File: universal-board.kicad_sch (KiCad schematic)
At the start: 47 parts, among them J1 USB_C_Receptacle, J2 Conn_02x04_Odd_Even, J3 Conn_01x08, J4 CONN_WS2812, J5 CONN_I2C_GROVE, Q1 BSS138, SW1 SW_RESET, SW2 SW_ACK, U1 USBLC6-2SC6, U2 AMS1117-3.3, U3 CH224K, U4 USBLC6-2SC6, U5 74AHCT1G125, U6 TSOP384xx, U7 ESP32-S3-WROOM-1

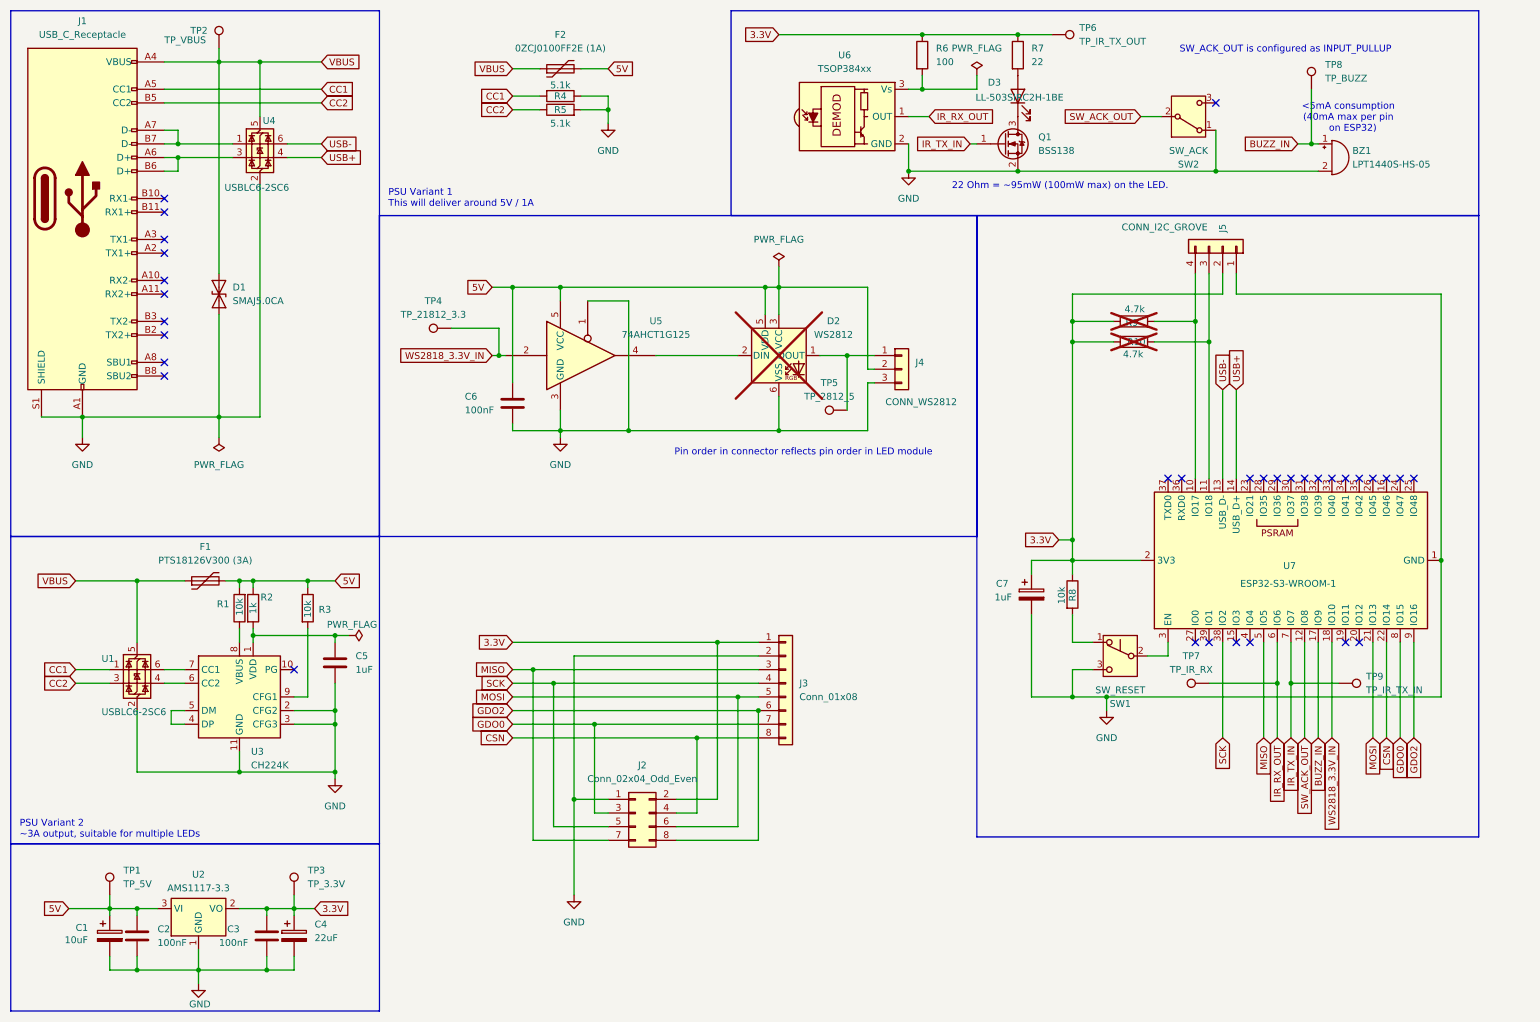
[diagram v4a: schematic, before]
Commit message: Added UART for HLK modules.
Updated TODO.
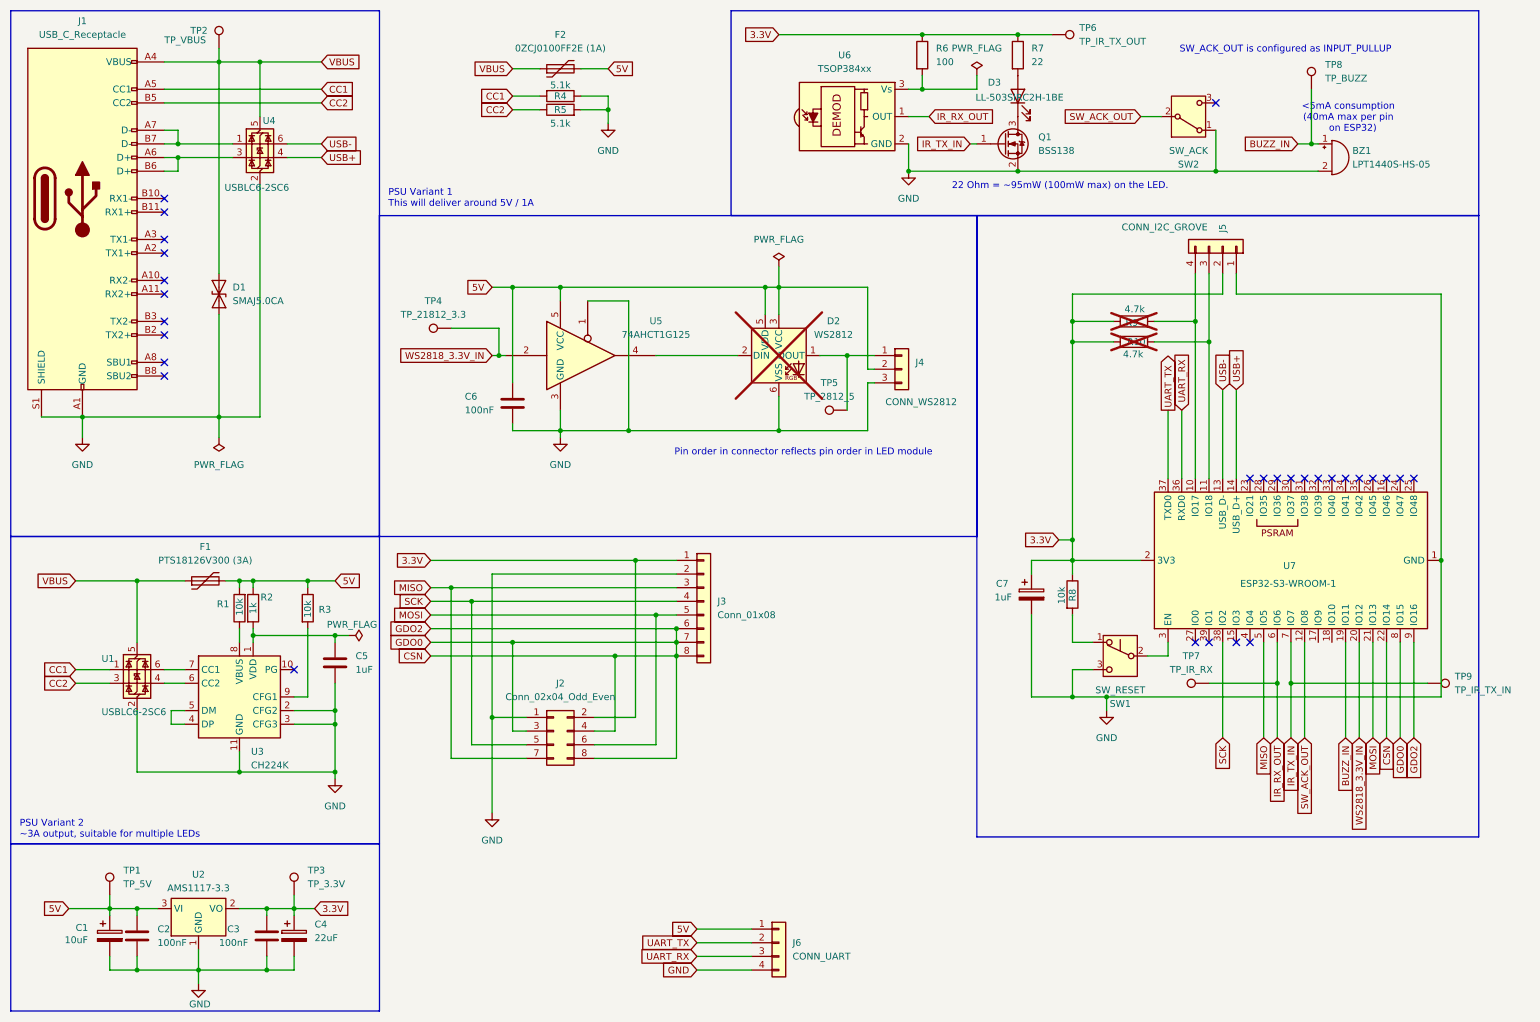
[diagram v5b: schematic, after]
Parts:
- added J6: CONN_UART, symbol Connector_Generic:Conn_01x04
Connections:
- net GDO0 is gone; now on net CSN: J2.3 (Pin_3), J3.7 (Pin_7), U7.8 (IO15)
- net GDO2 is gone; now on net CSN: J2.8 (Pin_8), J3.6 (Pin_6), U7.9 (IO16)
- net 5V: now also J6.1 (Pin_1)
- net BUZZ_IN: now also U7.19 (IO11); no longer U7.17 (IO9)
- net GND: now also J6.4 (Pin_4)
- net WS2818_3.3V_IN: now also U7.20 (IO12); no longer U7.18 (IO10)
- net UART_RX: now reaches U7.36 (RXD0)
- net UART_RX: now also J6.3 (Pin_3)
- net UART_TX: now reaches U7.37 (TXD0)
- net UART_TX: now also J6.2 (Pin_2)
- no-connect marks 33 -> 29
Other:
- moved on the sheet: J2, J3, TP9

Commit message: Changed resistor footprints to be actual resistors.
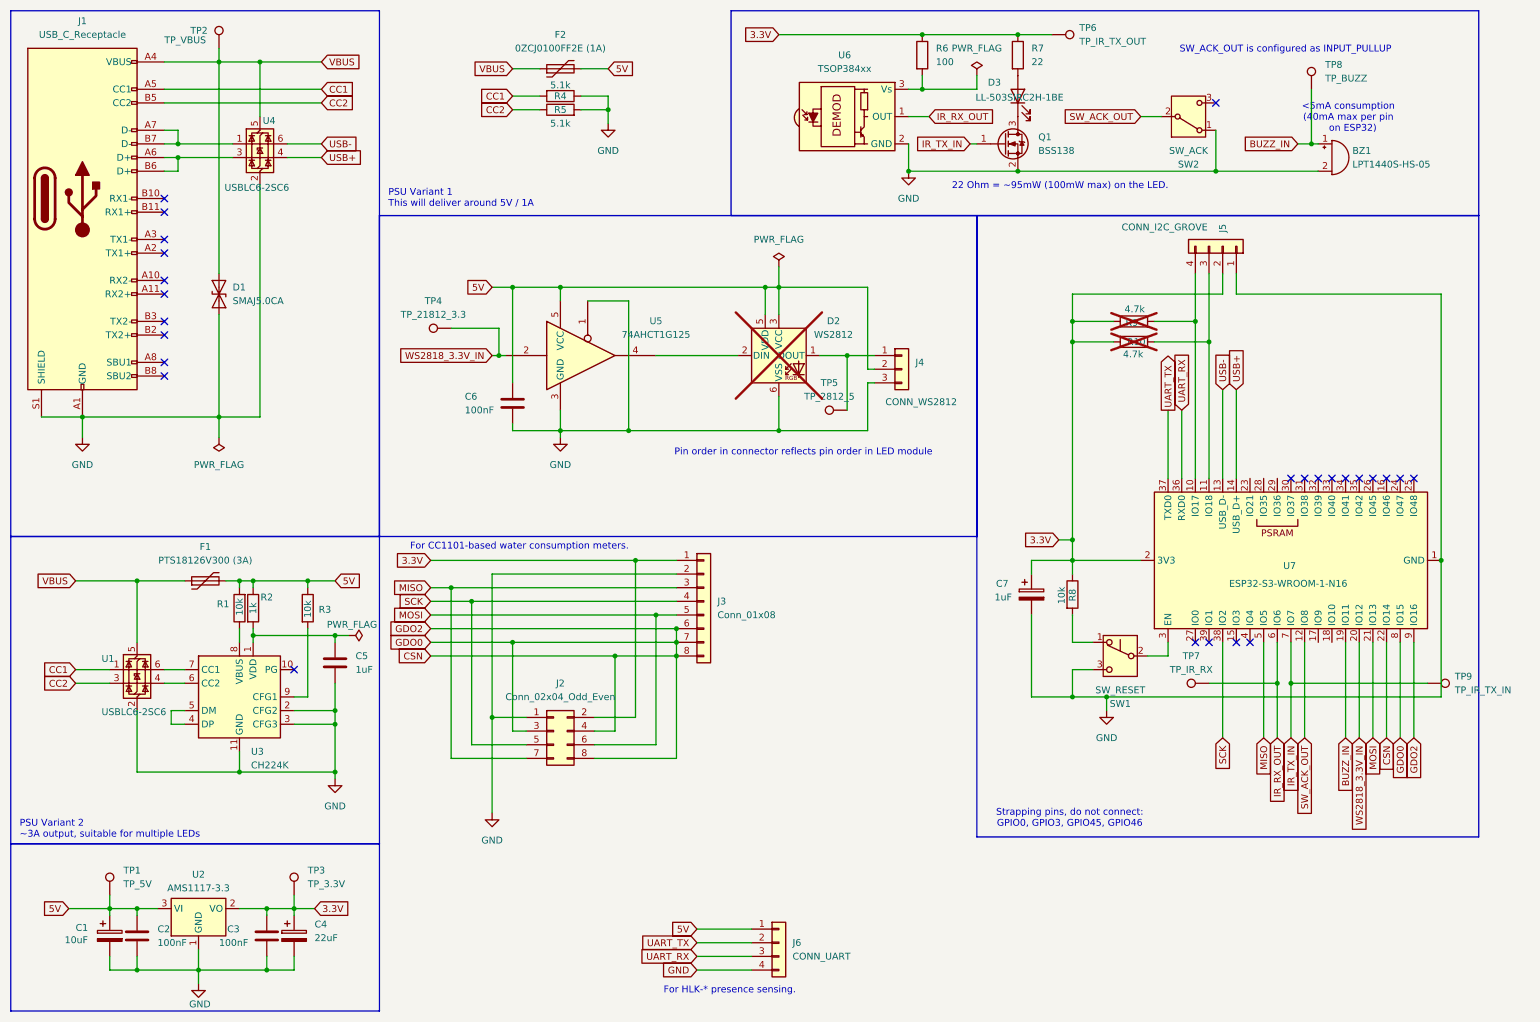
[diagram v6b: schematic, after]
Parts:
- R1, R10, R2, R3, R4, R5, R6, R7, R8, R9: footprint Capacitor_SMD:C_1206_3216Metric_Pad1.33x1.80mm_HandSolder -> Resistor_SMD:R_1206_3216Metric_Pad1.30x1.75mm_HandSolder
- U7: value ESP32-S3-WROOM-1 -> ESP32-S3-WROOM-1-N16
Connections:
- no-connect marks 29 -> 26
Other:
- note added: "For CC1101-based water consumption meters."
- note added: "For HLK-* presence sensing."
- note added: "Strapping pins, do not connect: GPIO0, GPIO3, GPIO45, GPIO46"
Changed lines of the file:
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@@
 		)
 	)
+	(text "For CC1101-based water consumption meters."
+		(exclude_from_sim no)
+		(at 106.68 111.76 0)
+		(effects
+			(font
+				(size 1.27 1.27)
+			)
+		)
+	)
 	(text "<5mA consumption\n(40mA max per pin\n   on ESP32)\n"
 		(exclude_from_sim no)
@@
 		)
 	)
+	(text "Strapping pins, do not connect:\nGPIO0, GPIO3, GPIO45, GPIO46"
+		(exclude_from_sim no)
+		(at 209.042 162.306 0)
+		(effects
+			(font
+				(size 1.27 1.27)
+			)
+		)
+	)
+	(text "For HLK-* presence sensing."
+		(exclude_from_sim no)
+		(at 145.796 194.31 0)
+		(effects
+			(font
+				(size 1.27 1.27)
+			)
+		)
+	)
 	(text "Pin order in connector reflects pin order in LED module"
 		(exclude_from_sim no)
@@
 	)
 	(no_connect
-		(at 247.65 99.06)
-	)
-	(no_connect
 		(at 267.97 99.06)
 	)
 	(no_connect
-		(at 245.11 99.06)
-	)
-	(no_connect
 		(at 40.64 72.39)
 	)
@@
 		(at 240.03 129.54)
 	)
-	(no_connect
-		(at 242.57 99.06)
-	)
 	(wire
 		(pts
@@
 			)
 		)
-		(property "Footprint" "Capacitor_SMD:C_1206_3216Metric_Pad1.33x1.80mm_HandSolder"
+		(property "Footprint" "Resistor_SMD:R_1206_3216Metric_Pad1.30x1.75mm_HandSolder"
 			(at 207.772 120.65 90)
 			(effects
@@
 			)
 		)
-		(property "Footprint" "Capacitor_SMD:C_1206_3216Metric_Pad1.33x1.80mm_HandSolder"
+		(property "Footprint" "Resistor_SMD:R_1206_3216Metric_Pad1.30x1.75mm_HandSolder"
 			(at 197.612 20.32 90)
 			(effects
@@
 			)
 		)
-		(property "Footprint" "Capacitor_SMD:C_1206_3216Metric_Pad1.33x1.80mm_HandSolder"
+		(property "Footprint" "Resistor_SMD:R_1206_3216Metric_Pad1.30x1.75mm_HandSolder"
 			(at 55.372 123.19 90)
 			(effects
@@
 			)
 		)
-		(property "Value" "ESP32-S3-WROOM-1"
+		(property "Value" "ESP32-S3-WROOM-1-N16"
 			(at 249.682 118.618 90)
 			(effects
@@
 			)
 		)
-		(property "Footprint" "Capacitor_SMD:C_1206_3216Metric_Pad1.33x1.80mm_HandSolder"
+		(property "Footprint" "Resistor_SMD:R_1206_3216Metric_Pad1.30x1.75mm_HandSolder"
 			(at 220.98 71.628 90)
 			(effects
@@
 			)
 		)
-		(property "Footprint" "Capacitor_SMD:C_1206_3216Metric_Pad1.33x1.80mm_HandSolder"
+		(property "Footprint" "Resistor_SMD:R_1206_3216Metric_Pad1.30x1.75mm_HandSolder"
 			(at 220.98 71.882 90)
 			(effects
@@
 			)
 		)
-		(property "Footprint" "Capacitor_SMD:C_1206_3216Metric_Pad1.33x1.80mm_HandSolder"
+		(property "Footprint" "Resistor_SMD:R_1206_3216Metric_Pad1.30x1.75mm_HandSolder"
 			(at 56.388 123.19 90)
 			(effects
@@
 			)
 		)
-		(property "Footprint" "Capacitor_SMD:C_1206_3216Metric_Pad1.33x1.80mm_HandSolder"
+		(property "Footprint" "Resistor_SMD:R_1206_3216Metric_Pad1.30x1.75mm_HandSolder"
 			(at 114.3 32.258 90)
 			(effects
@@
 			)
 		)
-		(property "Footprint" "Capacitor_SMD:C_1206_3216Metric_Pad1.33x1.80mm_HandSolder"
+		(property "Footprint" "Resistor_SMD:R_1206_3216Metric_Pad1.30x1.75mm_HandSolder"
 			(at 114.3 26.162 90)
 			(effects
@@
 			)
 		)
-		(property "Footprint" "Capacitor_SMD:C_1206_3216Metric_Pad1.33x1.80mm_HandSolder"
+		(property "Footprint" "Resistor_SMD:R_1206_3216Metric_Pad1.30x1.75mm_HandSolder"
 			(at 179.832 20.32 90)
 			(effects
@@
 			)
 		)
-		(property "Footprint" "Capacitor_SMD:C_1206_3216Metric_Pad1.33x1.80mm_HandSolder"
+		(property "Footprint" "Resistor_SMD:R_1206_3216Metric_Pad1.30x1.75mm_HandSolder"
 			(at 65.532 123.19 90)
 			(effects

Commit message: Added footprint for GCT USB4105-GF-A
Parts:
- J1: footprint Connector_USB:USB_C_Receptacle_GCT_USB4085 -> Connector_USB:USB_C_Receptacle_GCT_USB4105-xx-A_16P_TopMnt_Horizontal
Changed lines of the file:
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@@
 			)
 		)
-		(property "Footprint" "Connector_USB:USB_C_Receptacle_GCT_USB4085"
+		(property "Footprint" "Connector_USB:USB_C_Receptacle_GCT_USB4105-xx-A_16P_TopMnt_Horizontal"
 			(at 29.21 46.99 0)
 			(effects

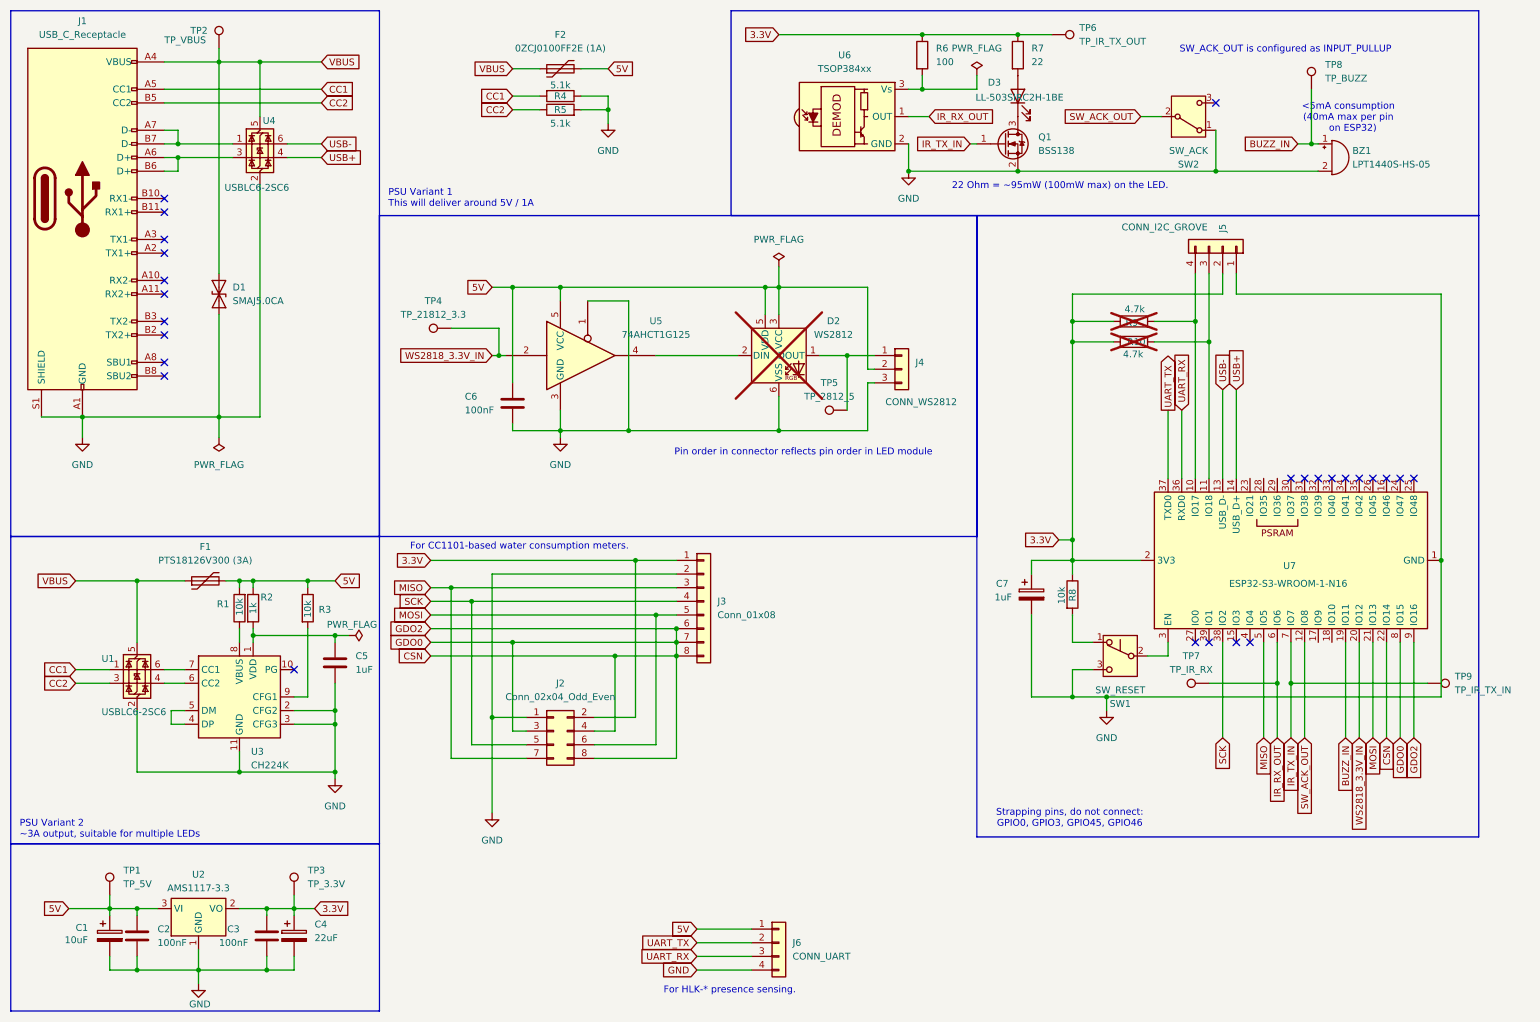
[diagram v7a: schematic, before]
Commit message: DRC passes on schematic.
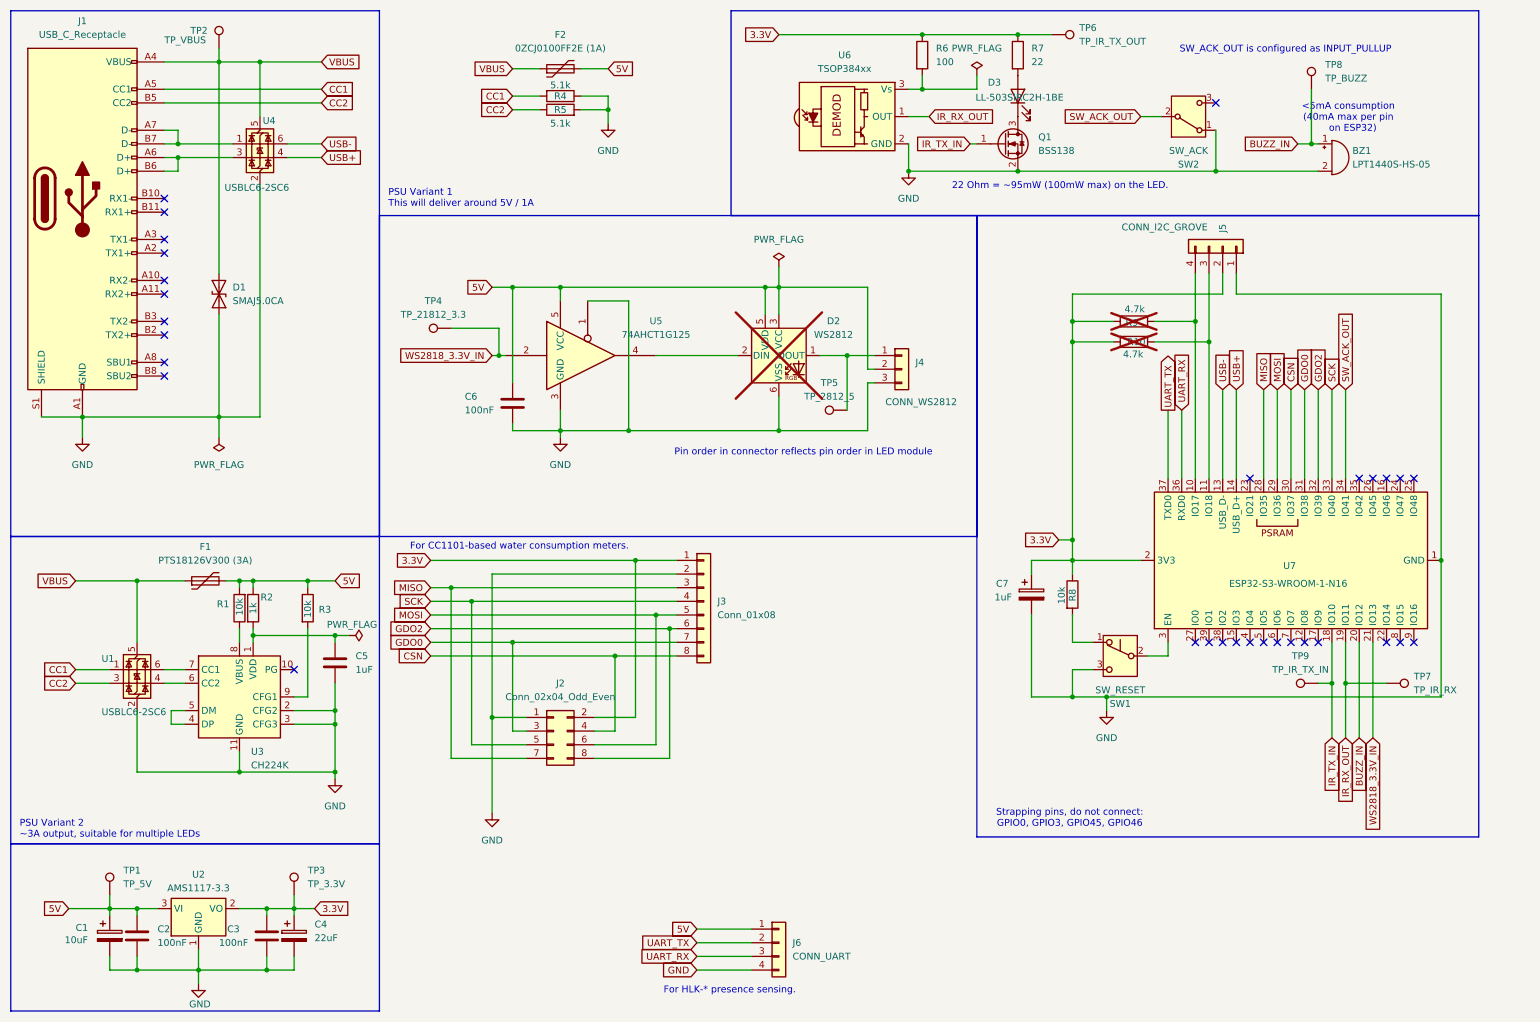
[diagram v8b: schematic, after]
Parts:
- BZ1: footprint Buzzer_Beeper:MagneticBuzzer_CUI_CST-931RP-A -> Buzzer_Beeper:Buzzer_Mallory_AST1109MLTRQ
- J6: footprint (none) -> Connector_PinHeader_2.54mm:PinHeader_1x04_P2.54mm_Vertical
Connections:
- net BUZZ_IN: now also U7.20 (IO12); no longer U7.19 (IO11)
- net CSN: now also U7.30 (IO37); no longer J2.3 (Pin_3), J2.8 (Pin_8), J3.6 (Pin_6), J3.7 (Pin_7), U7.22 (IO14), U7.8 (IO15), U7.9 (IO16)
- net IR_RX_OUT: now also U7.19 (IO11); no longer U7.6 (IO6)
- net IR_TX_IN: now also U7.18 (IO10); no longer U7.7 (IO7)
- net MISO: now also U7.28 (IO35); no longer U7.5 (IO5)
- net MOSI: now also U7.29 (IO36); no longer U7.21 (IO13)
- net SCK: now also U7.33 (IO40); no longer U7.38 (IO2)
- net SW_ACK_OUT: now also U7.34 (IO41); no longer U7.12 (IO8)
- net WS2818_3.3V_IN: now also U7.21 (IO13); no longer U7.20 (IO12)
- net GDO0: now reaches U7.31 (IO38)
- net GDO0: now also J2.3 (Pin_3), J3.7 (Pin_7)
- net GDO2: now reaches U7.32 (IO39)
- net GDO2: now also J2.8 (Pin_8), J3.6 (Pin_6)
- no-connect marks 26 -> 31
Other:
- moved on the sheet: TP7, TP9
